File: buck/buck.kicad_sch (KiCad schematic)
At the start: 15 parts, among them IC1 TPS630702RNMR

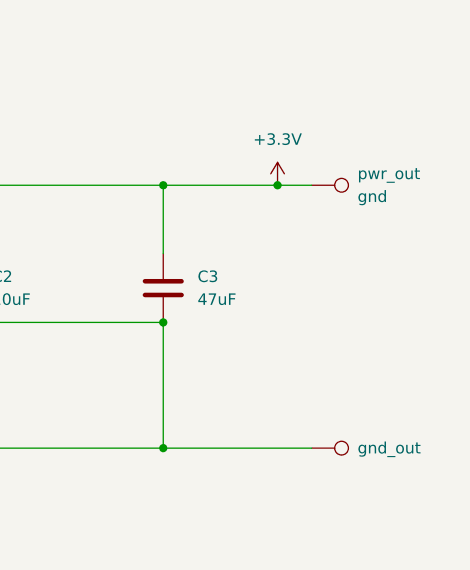
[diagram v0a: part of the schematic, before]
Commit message: slight fixes
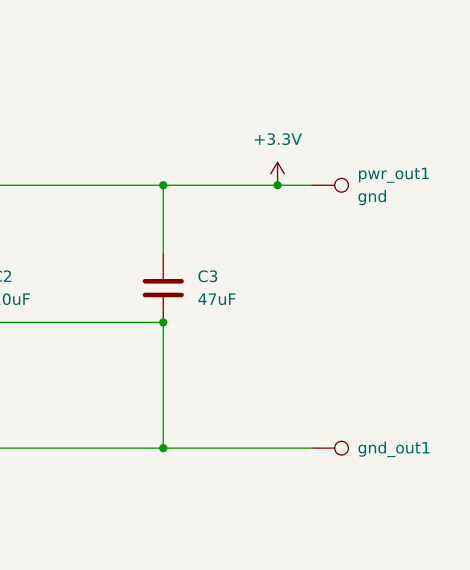
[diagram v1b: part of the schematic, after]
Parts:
- EN1, gnd1, pwr1: footprint TestPoint:TestPoint_Pad_1.0x1.0mm -> TestPoint:TestPoint_THTPad_1.0x1.0mm_Drill0.5mm
- gnd_out1: renamed from gnd_out; footprint TestPoint:TestPoint_Pad_1.0x1.0mm -> TestPoint:TestPoint_THTPad_1.0x1.0mm_Drill0.5mm
- pwr_out1: renamed from pwr_out; footprint TestPoint:TestPoint_Pad_1.0x1.0mm -> TestPoint:TestPoint_THTPad_1.0x1.0mm_Drill0.5mm
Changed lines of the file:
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@@
 		(dnp no)
 		(fields_autoplaced yes)
-		(property "Reference" "gnd_out"
+		(property "Reference" "gnd_out1"
 			(at 270.51 104.1399 90)
 			(effects
@@
 			)
 		)
-		(property "Footprint" "TestPoint:TestPoint_Pad_1.0x1.0mm"
+		(property "Footprint" "TestPoint:TestPoint_THTPad_1.0x1.0mm_Drill0.5mm"
 			(at 265.43 109.22 0)
 			(effects
@@
 			(project "buck"
 				(path "/09b05005-515b-4cb8-8c28-d9a88da80a5e"
-					(reference "gnd_out")
+					(reference "gnd_out1")
 					(unit 1)
 				)
@@
 			)
 		)
-		(property "Footprint" "TestPoint:TestPoint_Pad_1.0x1.0mm"
+		(property "Footprint" "TestPoint:TestPoint_THTPad_1.0x1.0mm_Drill0.5mm"
 			(at 99.06 91.44 0)
 			(effects
@@
 			)
 		)
-		(property "Footprint" "TestPoint:TestPoint_Pad_1.0x1.0mm"
+		(property "Footprint" "TestPoint:TestPoint_THTPad_1.0x1.0mm_Drill0.5mm"
 			(at 78.74 73.66 0)
 			(effects
@@
 		(dnp no)
 		(fields_autoplaced yes)
-		(property "Reference" "pwr_out"
+		(property "Reference" "pwr_out1"
 			(at 270.51 73.6599 90)
 			(effects
@@
 			)
 		)
-		(property "Footprint" "TestPoint:TestPoint_Pad_1.0x1.0mm"
+		(property "Footprint" "TestPoint:TestPoint_THTPad_1.0x1.0mm_Drill0.5mm"
 			(at 265.43 80.01 0)
 			(effects
@@
 			(project "buck"
 				(path "/09b05005-515b-4cb8-8c28-d9a88da80a5e"
-					(reference "pwr_out")
+					(reference "pwr_out1")
 					(unit 1)
 				)
@@
 			)
 		)
-		(property "Footprint" "TestPoint:TestPoint_Pad_1.0x1.0mm"
+		(property "Footprint" "TestPoint:TestPoint_THTPad_1.0x1.0mm_Drill0.5mm"
 			(at 78.74 99.06 0)
 			(effects
